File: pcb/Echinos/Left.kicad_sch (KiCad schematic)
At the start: 29 parts, among them J1 USB_C_Receptacle_USB2.0, J2 FPC (PCB), J206 Conn_01x06_Pin, J4 FPC_VIK, J5 SATA-7p, U3 SRV05-4, U5 XC6210B332MR-G, U7 SRV05-4

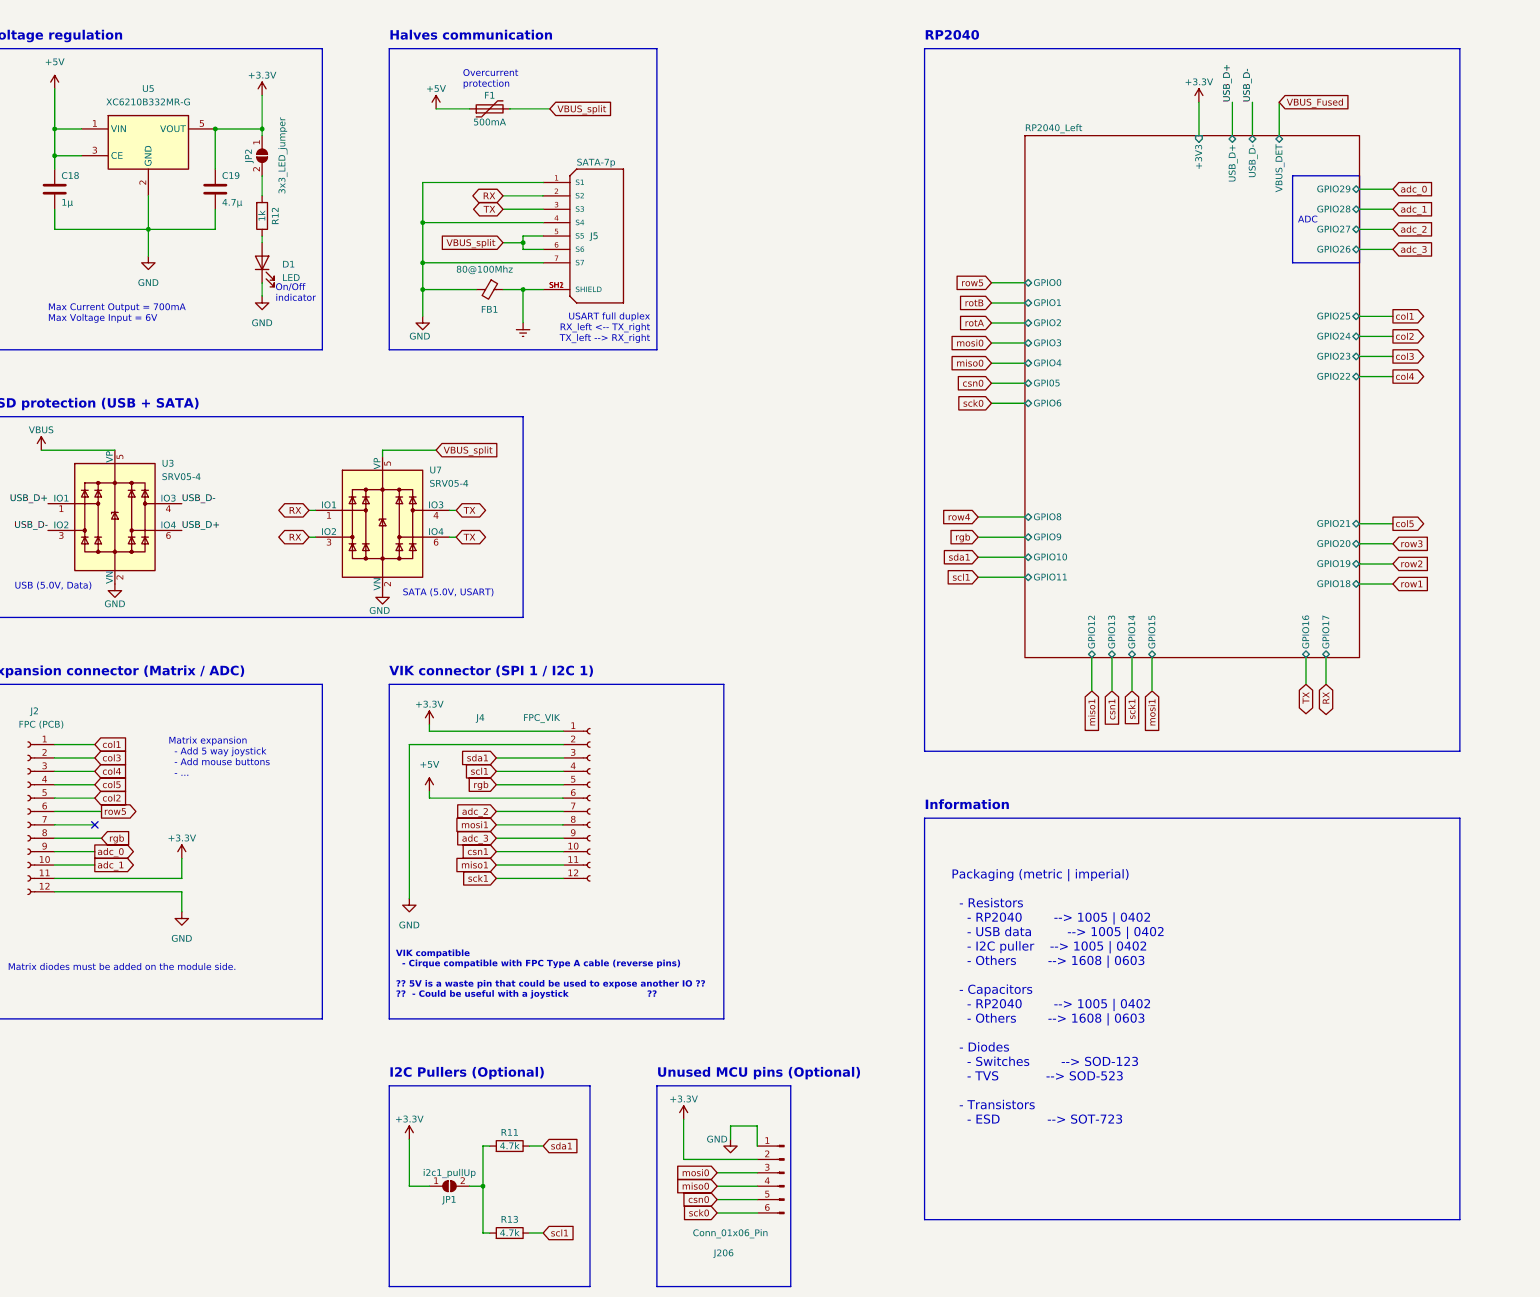
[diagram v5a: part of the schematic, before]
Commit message: 🚸 💥 🏗️ [PCB] - Start improving overall MCU routing to be able to make space for headers (SPI, Joystick, ...). USB + FLASH + VIK + DET + 5V --> 3.3V + ROW + COL
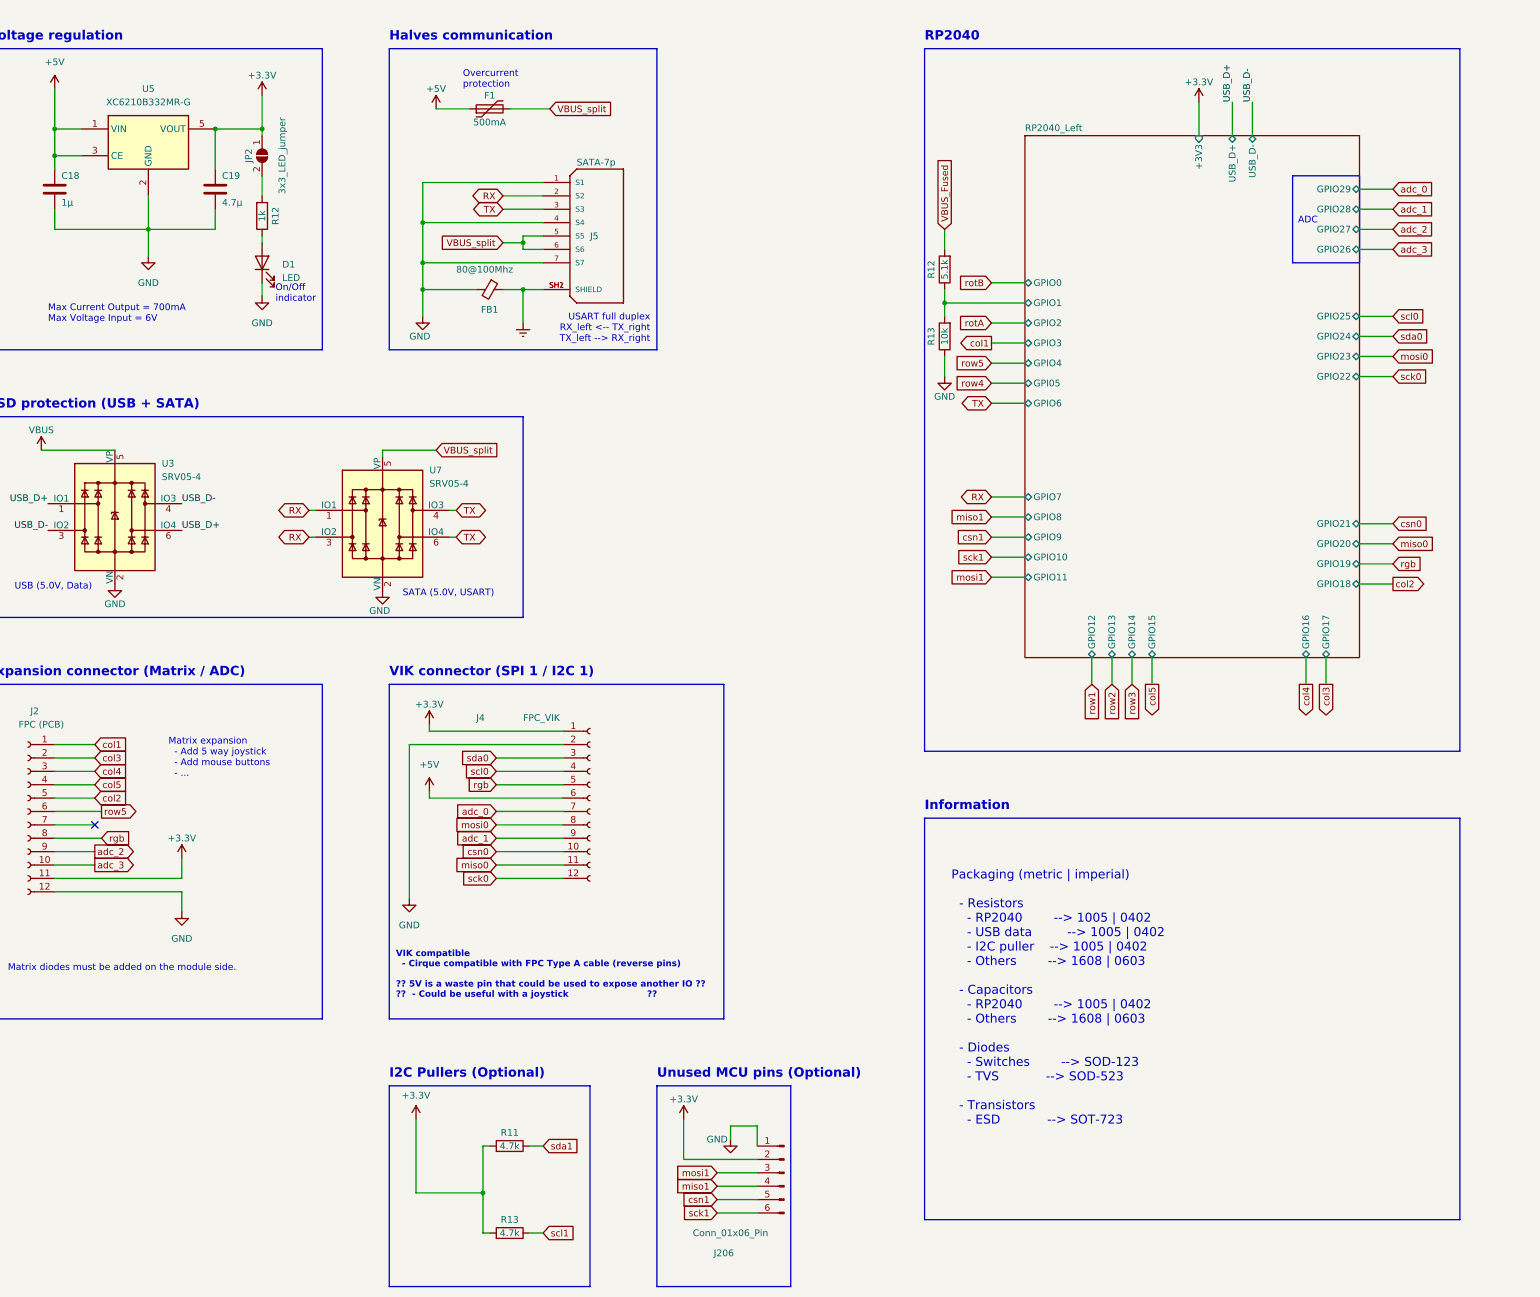
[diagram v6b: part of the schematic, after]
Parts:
- removed JP1: i2c1_pullUp, Echinos:SolderJumper_Open_0.8x1.2mm, symbol Jumper:SolderJumper_2_Open
- added R12: 5.1k, Resistor_SMD:R_0402_1005Metric_Pad0.72x0.64mm_HandSolder, symbol Device:R
- added R13: 10k, Resistor_SMD:R_0402_1005Metric_Pad0.72x0.64mm_HandSolder, symbol Device:R
- R11, R13: footprint Resistor_SMD:R_0402_1005Metric_Pad0.72x0.64mm_HandSolder -> Resistor_SMD:R_0805_2012Metric_Pad1.20x1.40mm_HandSolder; LCSC C25900 -> (none)
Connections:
- net +3.3V: now also R11.2, R13.2
- net GND: now also R13.1
- net VBUS_Fused: now also R12.2
- net adc_0: now also J4.7 (Pin_7); no longer J2.9 (Pin_9)
- net adc_1: now also J4.9 (Pin_9); no longer J2.10 (Pin_10)
- net adc_2: now also J2.9 (Pin_9); no longer J4.7 (Pin_7)
- net adc_3: now also J2.10 (Pin_10); no longer J4.9 (Pin_9)
- net csn0: now also J4.10 (Pin_10); no longer J206.5 (Pin_5)
- net csn1: now also J206.5 (Pin_5); no longer J4.10 (Pin_10)
- net miso0: now also J4.11 (Pin_11); no longer J206.4 (Pin_4)
- net miso1: now also J206.4 (Pin_4); no longer J4.11 (Pin_11)
- net mosi0: now also J4.8 (Pin_8); no longer J206.3 (Pin_3)
- net mosi1: now also J206.3 (Pin_3); no longer J4.8 (Pin_8)
- net sck0: now also J4.12 (Pin_12); no longer J206.6 (Pin_6)
- net sck1: now also J206.6 (Pin_6); no longer J4.12 (Pin_12)
- net scl1: no longer J4.4 (Pin_4)
- net sda1: no longer J4.3 (Pin_3)
- new net RP2040_Left/GPIO1: R12.1, R13.2
- new net scl0: J4.4 (Pin_4)
- new net sda0: J4.3 (Pin_3)
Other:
- sheet RP2040_Left ports: added GPIO7; removed VBUS_DET

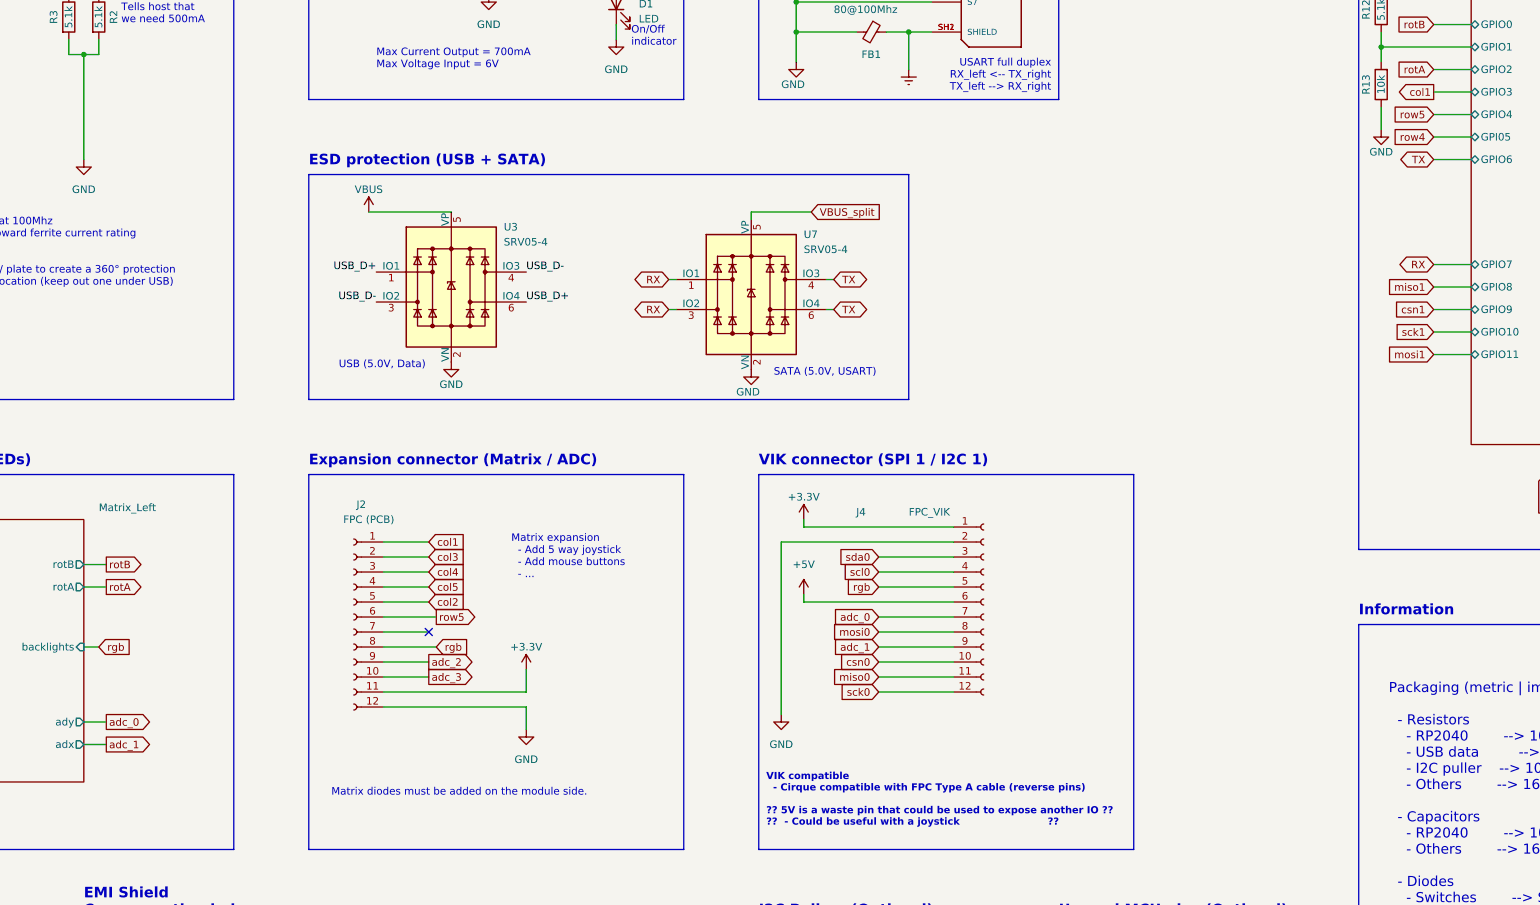
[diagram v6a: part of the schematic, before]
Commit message: 🚸 💥 🏗️ [PCB] - Improving overall MCU routing to be able to make space for headers (SPI, Joystick, ...). SATA - DEBUG - IO(analog) - IO(spi/matrix) - OSCILLATOR -
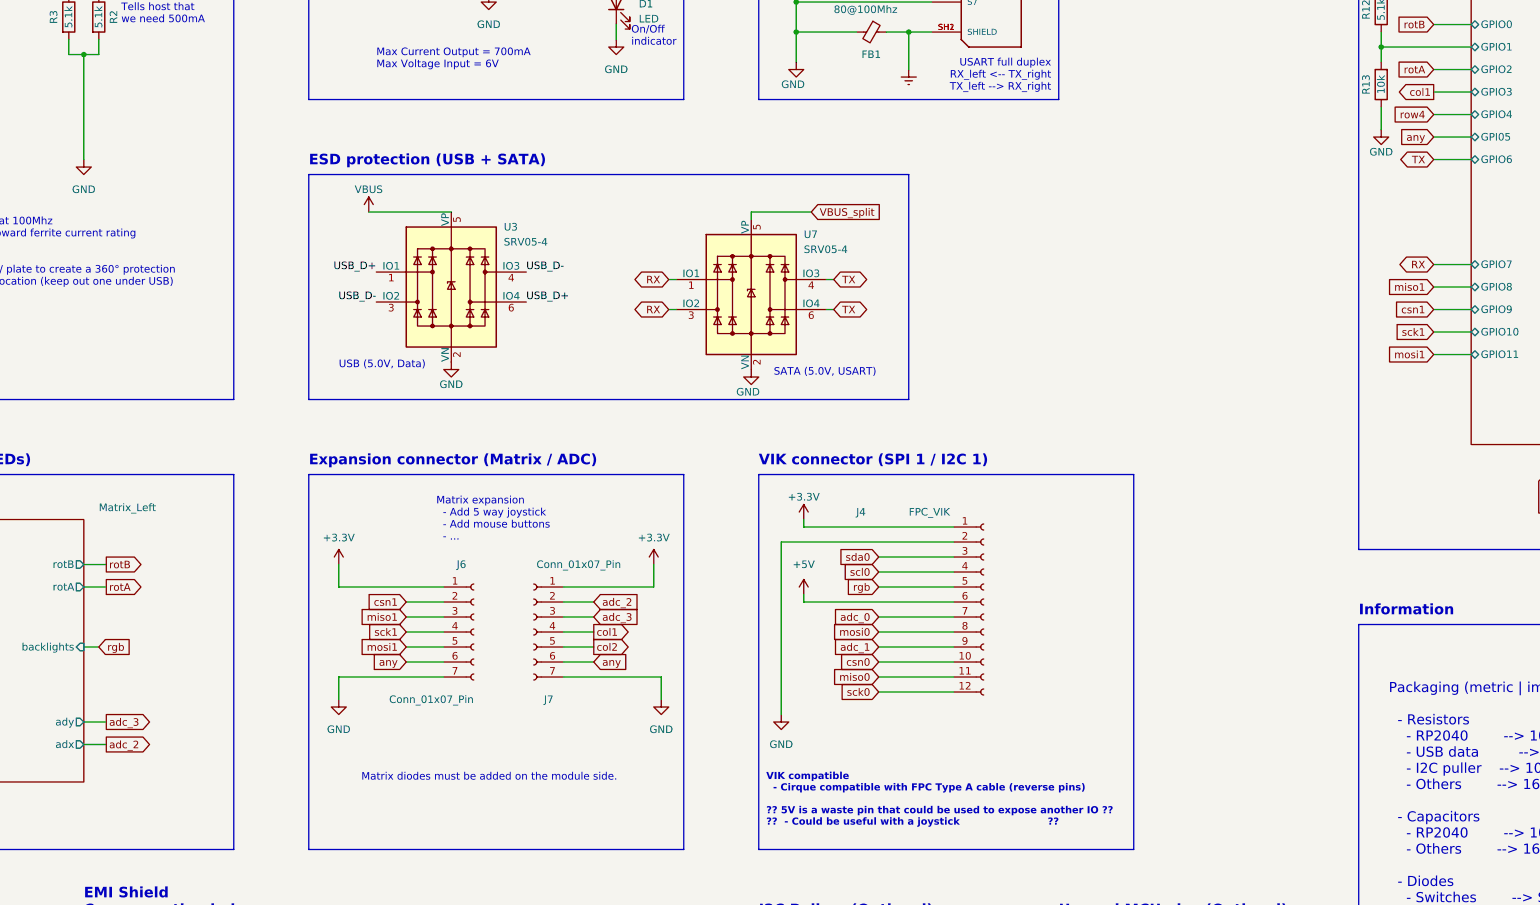
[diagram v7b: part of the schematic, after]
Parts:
- removed J2: FPC (PCB), Connector_FFC-FPC:Hirose_FH12-12S-0.5SH_1x12-1MP_P0.50mm_Horizontal, symbol Connector:Conn_01x12_Socket
- added J6, J7: Conn_01x07_Pin, Connector_PinHeader_2.54mm:PinHeader_1x07_P2.54mm_Vertical, symbol Connector:Conn_01x07_Socket
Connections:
- net +3.3V: now also J6.1 (Pin_1), J7.1 (Pin_1)
- net GND: now also J6.7 (Pin_7), J7.7 (Pin_7)
- net adc_2: now also J7.2 (Pin_2)
- net adc_3: now also J7.3 (Pin_3)
- net col1: now also J7.4 (Pin_4)
- net col2: now also J7.5 (Pin_5)
- net csn1: now also J6.2 (Pin_2)
- net miso1: now also J6.3 (Pin_3)
- net mosi1: now also J6.5 (Pin_5)
- net sck1: now also J6.4 (Pin_4)
- new net any: J6.6 (Pin_6), J7.6 (Pin_6)
- no-connect marks 3 -> 2

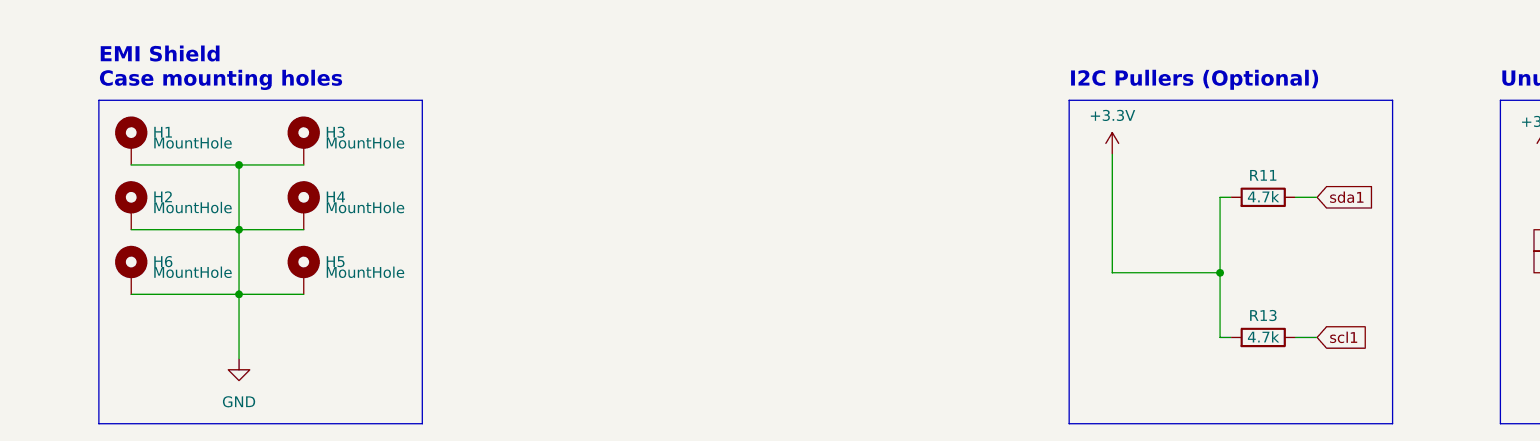
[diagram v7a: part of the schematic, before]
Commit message: ♻️ [PCB] - Connect I2C pull-ups (optional) and power to VIK. Improve routing especially for 5.0V and VBus. Add via stitching around power lines. Add ground plane. Unsure matching length between both USB differential pair (D+/D-). Remove unused mounting hole.
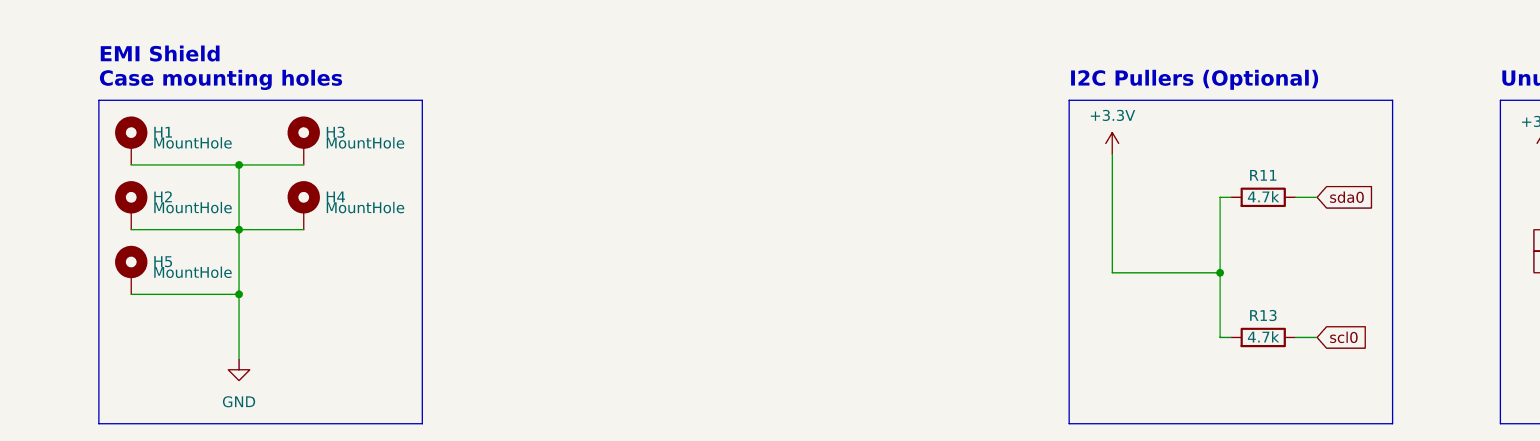
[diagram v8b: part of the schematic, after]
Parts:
- removed H5: MountHole, Echinos:MountingHole_3mm_Pad_Via, symbol Mechanical:MountingHole_Pad
- renumbered H6 to H5
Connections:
- net scl1 is gone; now on net scl0: R13.1
- net sda1 is gone; now on net sda0: R11.1
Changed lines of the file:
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@@
-    (stroke (width 0) (type default))
-  )
-  (wire (pts (xy 100.33 238.76) (xy 92.71 238.76))
     (stroke (width 0) (type default))
   )
@@
     )
   )
-  (global_label "sda1" (shape input) (at 219.71 227.33 0) (fields_autoplaced)
-    (effects (font (size 1.27 1.27)) (justify left))
-    (property "Intersheetrefs" "${INTERSHEET_REFS}" (at 227.1514 227.33 0)
+  (global_label "sda0" (shape input) (at 219.71 227.33 0) (fields_autoplaced)
+    (effects (font (size 1.27 1.27)) (justify left))
+    (property "Intersheetrefs" "${INTERSHEET_REFS}" (at 227.2308 227.33 0)
       (effects (font (size 1.27 1.27)) (justify left) hide)
     )
@@
     )
   )
-  (global_label "scl1" (shape input) (at 219.71 243.84 0) (fields_autoplaced)
-    (effects (font (size 1.27 1.27)) (justify left))
-    (property "Intersheetrefs" "${INTERSHEET_REFS}" (at 226.6072 243.84 0)
+  (global_label "scl0" (shape input) (at 219.71 243.84 0) (fields_autoplaced)
+    (effects (font (size 1.27 1.27)) (justify left))
+    (property "Intersheetrefs" "${INTERSHEET_REFS}" (at 226.6866 243.84 0)
       (effects (font (size 1.27 1.27)) (justify left) hide)
     )
@@
         (path "/5bd3006d-ec09-4ffb-bec3-03fa5613b46a/82089e05-aeac-4bc0-b466-29ce28ef1ab1"
           (reference "J206") (unit 1)
-        )
-      )
-    )
-  )
-  (symbol (lib_id "Mechanical:MountingHole_Pad") (at 100.33 236.22 0) (unit 1)
-    (in_bom no) (on_board yes) (dnp no)
-    (property "Reference" "H5" (at 102.87 234.95 0)
-      (effects (font (size 1.27 1.27)) (justify left))
-    )
-    (property "Value" "MountHole" (at 102.87 236.22 0)
-      (effects (font (size 1.27 1.27)) (justify left))
-    )
-    (property "Footprint" "Echinos:MountingHole_3mm_Pad_Via" (at 100.33 236.22 0)
-      (effects (font (size 1.27 1.27)) hide)
-    )
-    (property "Datasheet" "~" (at 100.33 236.22 0)
-      (effects (font (size 1.27 1.27)) hide)
-    )
-    (pin "1")
-    (instances
-      (project "Echinos"
-        (path "/5bd3006d-ec09-4ffb-bec3-03fa5613b46a/82089e05-aeac-4bc0-b466-29ce28ef1ab1"
-          (reference "H5") (unit 1)
         )
       )
@@
   (symbol (lib_id "Mechanical:MountingHole_Pad") (at 80.01 236.22 0) (unit 1)
     (in_bom no) (on_board yes) (dnp no)
-    (property "Reference" "H6" (at 82.55 234.95 0)
+    (property "Reference" "H5" (at 82.55 234.95 0)
       (effects (font (size 1.27 1.27)) (justify left))
     )
@@
       (project "Echinos"
         (path "/5bd3006d-ec09-4ffb-bec3-03fa5613b46a/82089e05-aeac-4bc0-b466-29ce28ef1ab1"
-          (reference "H6") (unit 1)
-        )
-      )
+          (reference "H5") (unit 1)
+        )
+      )
